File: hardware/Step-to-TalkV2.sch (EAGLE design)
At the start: 19 parts, among them J1 Pogo Pad, J2 Pogo Pad, J3 Pogo Pad, J4 Pogo Pad, J5 Pogo Pad, J6 Pogo Pad, SW1 87438-02, U1 ATTINY85

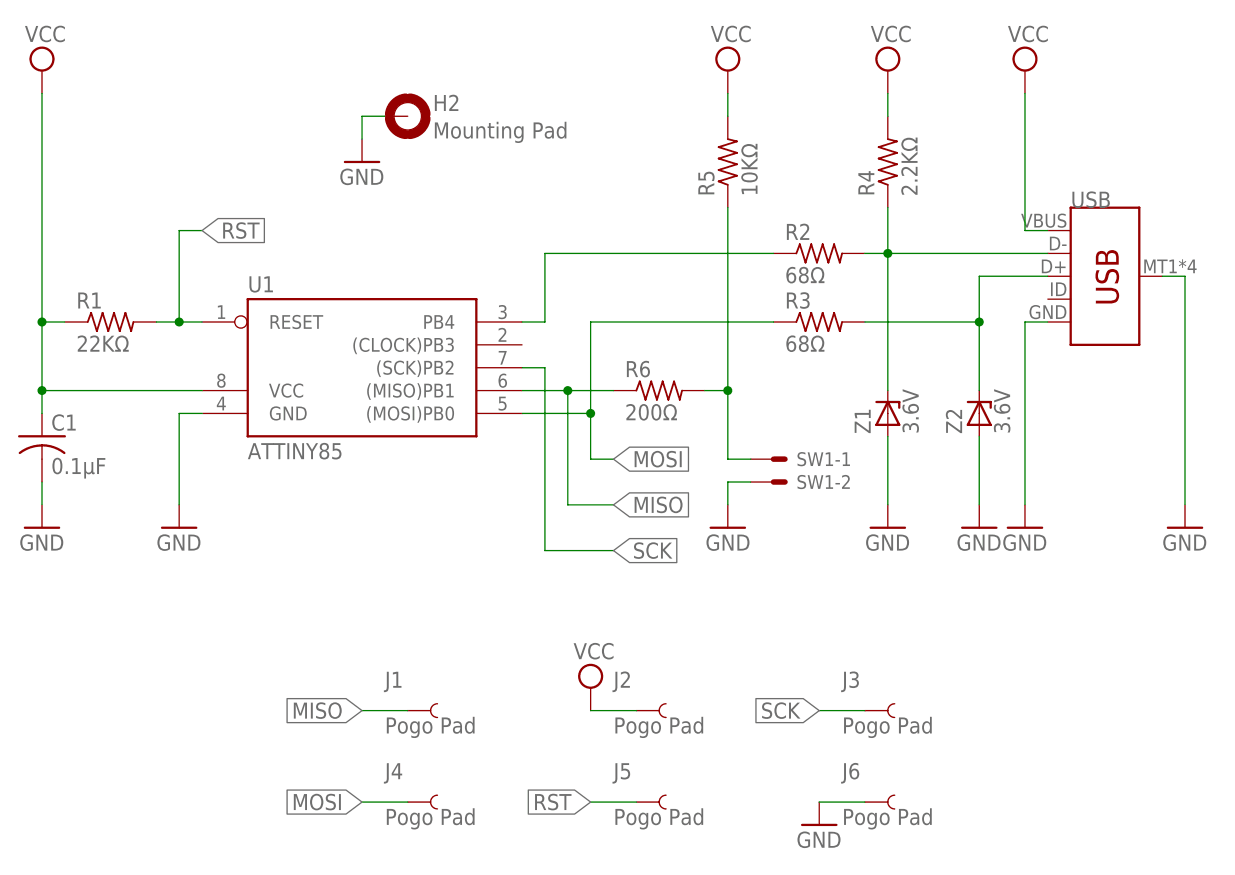
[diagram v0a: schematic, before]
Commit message: Optimize routing, increase diode pad size.
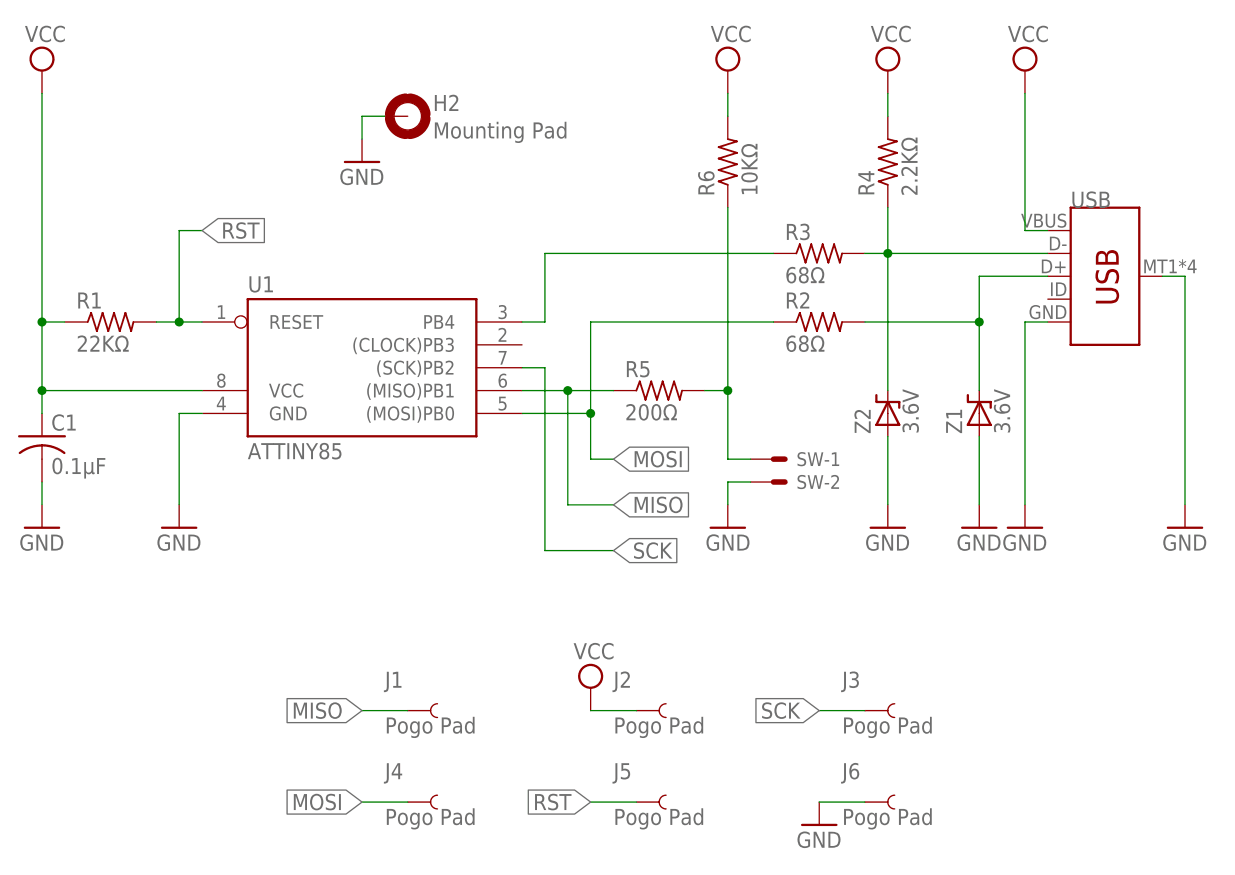
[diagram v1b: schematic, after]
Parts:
- R5: value 10KΩ -> 200Ω
- R6: value 200Ω -> 10KΩ
- Z1, Z2: device NXP_60_26022015:PESD5V0X1UB -> gjennings:BZT52C3V6TENLARGED
- renumbered SW1 to SW
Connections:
- net D+: now also R2.2, Z1.K; no longer R3.2, Z2.K
- net D-: now also R3.2, Z2.K; no longer R2.2, Z1.K
- net MISO: now also R5.1; no longer R6.1
- net MOSI: now also R2.1; no longer R3.1
- net N$2: now also R3.1; no longer R2.1
- net N$4: now also R5.2, R6.1; no longer R5.1, R6.2
- net VCC: now also R6.2; no longer R5.2
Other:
- moved on the sheet: R2, R3, R5, R6
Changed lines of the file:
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@@
 <part name="C1" library="adafruit" library_urn="urn:adsk.eagle:library:420" deviceset="C-US" device="C0603" value="0.1µF"/>
 <part name="R1" library="adafruit" library_urn="urn:adsk.eagle:library:420" deviceset="R-US_" device="R0603" value="22KΩ"/>
+<part name="R3" library="adafruit" library_urn="urn:adsk.eagle:library:420" deviceset="R-US_" device="R0603" value="68Ω"/>
 <part name="R2" library="adafruit" library_urn="urn:adsk.eagle:library:420" deviceset="R-US_" device="R0603" value="68Ω"/>
-<part name="R3" library="adafruit" library_urn="urn:adsk.eagle:library:420" deviceset="R-US_" device="R0603" value="68Ω"/>
 <part name="R4" library="adafruit" library_urn="urn:adsk.eagle:library:420" deviceset="R-US_" device="R0603" value="2.2KΩ"/>
 <part name="SUPPLY1" library="supply2" library_urn="urn:adsk.eagle:library:372" deviceset="VCC" device=""/>
 <part name="GND1" library="supply1" library_urn="urn:adsk.eagle:library:371" deviceset="GND" device=""/>
-<part name="Z1" library="NXP_60_26022015" deviceset="PESD5V0X1UB" device="" value="3.6V"/>
-<part name="Z2" library="NXP_60_26022015" deviceset="PESD5V0X1UB" device="" value="3.6V"/>
+<part name="Z2" library="gjennings" deviceset="BZT52C3V6T" device="ENLARGED" value="3.6V"/>
+<part name="Z1" library="gjennings" deviceset="BZT52C3V6T" device="ENLARGED" value="3.6V"/>
 <part name="SUPPLY3" library="supply2" library_urn="urn:adsk.eagle:library:372" deviceset="VCC" device=""/>
 <part name="GND2" library="supply1" library_urn="urn:adsk.eagle:library:371" deviceset="GND" device=""/>
@@
 <part name="GND5" library="supply1" library_urn="urn:adsk.eagle:library:371" deviceset="GND" device=""/>
 <part name="U1" library="atmel" library_urn="urn:adsk.eagle:library:105" deviceset="TINY22" device="S" value="ATTINY85"/>
-<part name="R5" library="adafruit" library_urn="urn:adsk.eagle:library:420" deviceset="R-US_" device="R0603" value="10KΩ"/>
+<part name="R6" library="adafruit" library_urn="urn:adsk.eagle:library:420" deviceset="R-US_" device="R0603" value="10KΩ"/>
 <part name="USB" library="SparkFun-Connectors" deviceset="USB_MICRO-B" device="_SMT"/>
 <part name="SUPPLY5" library="supply2" library_urn="urn:adsk.eagle:library:372" deviceset="VCC" device=""/>
-<part name="R6" library="adafruit" library_urn="urn:adsk.eagle:library:420" deviceset="R-US_" device="R0603" value="200Ω"/>
+<part name="R5" library="adafruit" library_urn="urn:adsk.eagle:library:420" deviceset="R-US_" device="R0603" value="200Ω"/>
 <part name="GND6" library="supply1" library_urn="urn:adsk.eagle:library:371" deviceset="GND" device=""/>
 <part name="GND7" library="supply1" library_urn="urn:adsk.eagle:library:371" deviceset="GND" device=""/>
-<part name="SW1" library="con-molex" library_urn="urn:adsk.eagle:library:165" deviceset="87438-02" device="" value=""/>
+<part name="SW" library="con-molex" library_urn="urn:adsk.eagle:library:165" deviceset="87438-02" device="" value=""/>
 <part name="GND8" library="supply1" library_urn="urn:adsk.eagle:library:371" deviceset="GND" device=""/>
 <part name="H2" library="holes" library_urn="urn:adsk.eagle:library:237" deviceset="MOUNT-PAD-ROUND" device="4.3" value="Mounting Pad"/>
@@
 <instance part="C1" gate="G$1" x="-43.18" y="33.02"/>
 <instance part="R1" gate="G$1" x="-35.56" y="45.72"/>
-<instance part="R2" gate="G$1" x="43.18" y="53.34"/>
-<instance part="R3" gate="G$1" x="43.18" y="45.72"/>
+<instance part="R3" gate="G$1" x="43.18" y="53.34"/>
+<instance part="R2" gate="G$1" x="43.18" y="45.72"/>
 <instance part="R4" gate="G$1" x="50.8" y="63.5" rot="R90"/>
 <instance part="SUPPLY1" gate="G$1" x="-43.18" y="73.66"/>
 <instance part="GND1" gate="1" x="-43.18" y="22.86"/>
-<instance part="Z1" gate="G$1" x="50.8" y="35.56" rot="R90"/>
-<instance part="Z2" gate="G$1" x="60.96" y="35.56" rot="R90"/>
+<instance part="Z2" gate="G$1" x="50.8" y="35.56" rot="R90"/>
+<instance part="Z1" gate="G$1" x="60.96" y="35.56" rot="R90"/>
 <instance part="SUPPLY3" gate="G$1" x="50.8" y="73.66"/>
 <instance part="GND2" gate="1" x="60.96" y="22.86"/>
@@
 <instance part="GND5" gate="1" x="33.02" y="22.86" rot="MR0"/>
 <instance part="U1" gate="G$1" x="-7.62" y="40.64"/>
-<instance part="R5" gate="G$1" x="33.02" y="63.5" rot="R90"/>
+<instance part="R6" gate="G$1" x="33.02" y="63.5" rot="R90"/>
 <instance part="USB" gate="G$1" x="73.66" y="50.8"/>
 <instance part="SUPPLY5" gate="G$1" x="33.02" y="73.66"/>
-<instance part="R6" gate="G$1" x="25.4" y="38.1"/>
+<instance part="R5" gate="G$1" x="25.4" y="38.1"/>
 <instance part="GND6" gate="1" x="83.82" y="22.86"/>
 <instance part="GND7" gate="1" x="-27.94" y="22.86"/>
-<instance part="SW1" gate="-1" x="38.1" y="30.48"/>
-<instance part="SW1" gate="-2" x="38.1" y="27.94"/>
+<instance part="SW" gate="-1" x="38.1" y="30.48"/>
+<instance part="SW" gate="-2" x="38.1" y="27.94"/>
 <instance part="GND8" gate="1" x="-7.62" y="63.5"/>
 <instance part="H2" gate="G$1" x="-2.54" y="68.58"/>
@@
 </segment>
 <segment>
-<pinref part="Z1" gate="G$1" pin="A"/>
+<pinref part="Z2" gate="G$1" pin="A"/>
 <wire x1="50.8" y1="33.02" x2="50.8" y2="25.4" width="0.1524" layer="91"/>
 <pinref part="GND3" gate="1" pin="GND"/>
 </segment>
 <segment>
-<pinref part="Z2" gate="G$1" pin="A"/>
+<pinref part="Z1" gate="G$1" pin="A"/>
 <wire x1="60.96" y1="33.02" x2="60.96" y2="25.4" width="0.1524" layer="91"/>
 <pinref part="GND2" gate="1" pin="GND"/>
@@
 <wire x1="33.02" y1="27.94" x2="33.02" y2="25.4" width="0.1524" layer="91"/>
 <pinref part="GND5" gate="1" pin="GND"/>
-<pinref part="SW1" gate="-2" pin="S"/>
+<pinref part="SW" gate="-2" pin="S"/>
 </segment>
 <segment>
@@
 </segment>
 <segment>
-<pinref part="R5" gate="G$1" pin="2"/>
+<pinref part="R6" gate="G$1" pin="2"/>
 <pinref part="SUPPLY5" gate="G$1" pin="VCC"/>
 <wire x1="33.02" y1="68.58" x2="33.02" y2="71.12" width="0.1524" layer="91"/>
@@
 <net name="D-" class="0">
 <segment>
-<pinref part="R2" gate="G$1" pin="2"/>
+<pinref part="R3" gate="G$1" pin="2"/>
 <wire x1="48.26" y1="53.34" x2="50.8" y2="53.34" width="0.1524" layer="91"/>
-<pinref part="Z1" gate="G$1" pin="K"/>
+<pinref part="Z2" gate="G$1" pin="K"/>
 <wire x1="50.8" y1="53.34" x2="50.8" y2="38.1" width="0.1524" layer="91"/>
 <junction x="50.8" y="53.34"/>
@@
 <net name="D+" class="0">
 <segment>
-<pinref part="R3" gate="G$1" pin="2"/>
+<pinref part="R2" gate="G$1" pin="2"/>
 <wire x1="48.26" y1="45.72" x2="60.96" y2="45.72" width="0.1524" layer="91"/>
-<pinref part="Z2" gate="G$1" pin="K"/>
+<pinref part="Z1" gate="G$1" pin="K"/>
 <wire x1="60.96" y1="45.72" x2="60.96" y2="38.1" width="0.1524" layer="91"/>
 <pinref part="USB" gate="G$1" pin="D+"/>
@@
 <segment>
 <wire x1="33.02" y1="30.48" x2="35.56" y2="30.48" width="0.1524" layer="91"/>
-<pinref part="R5" gate="G$1" pin="1"/>
+<pinref part="R6" gate="G$1" pin="1"/>
 <wire x1="33.02" y1="30.48" x2="33.02" y2="38.1" width="0.1524" layer="91"/>
-<pinref part="R6" gate="G$1" pin="2"/>
+<pinref part="R5" gate="G$1" pin="2"/>
 <wire x1="33.02" y1="38.1" x2="33.02" y2="58.42" width="0.1524" layer="91"/>
 <wire x1="30.48" y1="38.1" x2="33.02" y2="38.1" width="0.1524" layer="91"/>
 <junction x="33.02" y="38.1"/>
-<pinref part="SW1" gate="-1" pin="S"/>
+<pinref part="SW" gate="-1" pin="S"/>
 </segment>
 </net>
@@
 <net name="N$2" class="0">
 <segment>
-<pinref part="R2" gate="G$1" pin="1"/>
+<pinref part="R3" gate="G$1" pin="1"/>
 <wire x1="38.1" y1="53.34" x2="12.7" y2="53.34" width="0.1524" layer="91"/>
 <wire x1="12.7" y1="53.34" x2="12.7" y2="45.72" width="0.1524" layer="91"/>
@@
 <net name="MOSI" class="0">
 <segment>
-<pinref part="R3" gate="G$1" pin="1"/>
+<pinref part="R2" gate="G$1" pin="1"/>
 <wire x1="38.1" y1="45.72" x2="17.78" y2="45.72" width="0.1524" layer="91"/>
 <wire x1="17.78" y1="45.72" x2="17.78" y2="35.56" width="0.1524" layer="91"/>
@@
 </segment>
 <segment>
-<pinref part="R6" gate="G$1" pin="1"/>
+<pinref part="R5" gate="G$1" pin="1"/>
 <pinref part="U1" gate="G$1" pin="(MISO)PB1"/>
 <wire x1="20.32" y1="38.1" x2="15.24" y2="38.1" width="0.1524" layer="91"/>
